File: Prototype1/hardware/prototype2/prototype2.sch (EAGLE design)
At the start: 79 parts, among them IC1 ATTINY13A-SSU, IC2 LDL112D33R, IC3 FT2232HL-REEL, IC4 93LC46BT-I_OT, U2 ESP-WROOM-32

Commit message: prototype 2 schema done(?)
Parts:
- added ATTINY13A: Header, connector:M06SILK_FEMALE_PTH
- added C2: 4.7 uF, passives:C-USC0805
- added C26, C27, C28, C29, C30, C31: 15 pF, passives:C-USC0805
- added C32: 0.1 uF, passives:C-USC0805
- added C33, C34: 10 uF, passives:C-USC0805
- added LED8: (no value), leds:LED3MM
- added R15, R18, R19, R20: 100 R, dc-26:RESISTOR0805-RES
- added R16: 4.7 K, passives:RESISTOR0805-RES
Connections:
- removed net N$12: C4.1, IC2.VIN, RESETTABLE_FUSE.2
- new net ATTINY_ESP_CON: IC1.[PCINT3/CLKI/ADC3]_PB3, R19.1
- new net ESP_ATTINY_CON: R19.2, U2.IO2
- new net ESP_LED1: R20.2, U2.IO16
- new net GPIO_APA104_DATA: IC1.[PCINT4/ADC2]_PB4, U$6.DIN
- new net N$35: U$6.DOUT, U$7.DIN
- new net N$36: U$7.DOUT, U$8.DIN
- new net N$37: U$8.DOUT, U$9.DIN
- new net N$38: U$10.DIN, U$9.DOUT
- new net N$39: U$10.DOUT, U$11.DIN
- new net N$9: LED8.A, R20.1
- new net PB0: ATTINY13A.4, IC1.PB0_[MOSI/AIN0/OC0A/PCINT0]
- new net PB1: ATTINY13A.5, IC1.PB1_[MISO/AIN1/OC0B/INT0/PCINT1]
- new net PB2: ATTINY13A.6, IC1.PB2_[SCK/ADC1/T0/PCINT2]
- new net PB3: ATTINY13A.2
- new net PB4: ATTINY13A.1
- new net PB5: ATTINY13A.3, IC1.PCINT5/!RESET!/ADC0/DW]_PB5, R16.1
- new net VBAT: C26.1, C27.1, C28.1, C29.1, C30.1, C31.1, C32.1, C33.1, C4.1, IC1.VCC, IC2.VIN, R16.2, RESETTABLE_FUSE.2, U$10.VDD, U$11.VDD, U$6.VDD, U$7.VDD, U$8.VDD, U$9.VDD
- net DISPLAY_BACKLIT: now also C34.1, R18.2; no longer U2.IO16
- net DISPLAY_RESET: now also C2.1, R15.2; no longer U2.IO2
- net GND: now also C2.2, C26.2, C27.2, C28.2, C29.2, C30.2, C31.2, C32.2, C33.2, C34.2, IC1.GND, LED8.C, U$10.GND, U$11.GND, U$6.GND, U$7.GND, U$8.GND, U$9.GND
- net VCC: now also R15.1, R18.1
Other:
- note added: "If we don't connect RESX line to a GPIO (and I'm not to save GPIO pins), we need to ensure RESX stay low for 10 us. So I'm going to set it up to stay low via a capacitor for 470 us by using a 4.7 uF cap and a 100 Ohm resistor calculator used: https://www.allaboutcircuits.com/tools/capacitor-Charge-and-time-constant-calculator/ same for back light, except using a larger cap to delay even longer"
- note removed: "If we use UART for badge pairing what pins do I use? Only pins left are input only Can I move MISO to one of these pins? so I can free up output pins? Need 2 more output Pins 1 for BADGE_PAIR_TX and 1 for ATTINY"
- moved on the sheet: IC1, U$10, U$11, U$6, U$7, U$8, U$9

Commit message: fixed erc errors and warnings
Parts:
- added J4: (no value), connector:M04PTH
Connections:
- removed net N$22: R2.1
- removed net N$23: C13.2
- removed net N$4: OFF/ON.S
- removed net PB3: ATTINY13A.2
- removed net PB4: ATTINY13A.1
- removed net PROX_RX: R14.1
- removed net RXD-SPI_PROM_MOSI: IC3.BDBUS1
- removed net SENSORVN: U2.SENSOR_VN
- removed net SENSORVP: U2.SENSOR_VP
- removed net TXD-SPI_PROM_CLK: IC3.BDBUS0
- new net SVN: J4.1, U2.SENSOR_VN
- new net SVP: J4.2, U2.SENSOR_VP
- net ATTINY_ESP_CON: now also ATTINY13A.2
- net GND: now also C25.2
- net GPIO_APA104_DATA: now also ATTINY13A.1
- net PAIR_RX: now also J4.4
- net PAIR_TX: now also J4.3
- net PROG_RX: now also R14.1
- net RXD_SPI_PROM_MOSI: now also IC3.BDBUS1
- net TXD_SPI_PROM_CLK: now also IC3.BDBUS0
- net VBAT: now also OFF/ON.S
- net VCC5V: now also C13.2, R2.1
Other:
- moved on the sheet: C13, C22, R2

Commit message: fixed one more warning
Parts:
- J4: value (none) -> DN PAIR
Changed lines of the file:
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@@
 <part name="LED8" library="leds" deviceset="LED" device="3MM"/>
 <part name="R20" library="dc-26" deviceset="RESISTOR" device="0805-RES" value="100 R"/>
-<part name="J4" library="connector" deviceset="M04" device="PTH"/>
+<part name="J4" library="connector" deviceset="M04" device="PTH" value="DN PAIR"/>
 </parts>
 <sheets>

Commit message: prototype 2 board design 'complete'
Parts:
- removed C30, C31: 15 pF, passives:C-USC0805
- removed U$10, U$11, U$6, U$7, U$8, U$9: APA-106, leds:APA-106
- added C35: 0.1 uF, passives:C-USC0805
- added IC5, IC6, IC7, IC8: APA104, leds:APA104
- R2: value 2 R -> 10 R
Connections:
- removed net N$35: U$6.DOUT, U$7.DIN
- removed net N$36: U$7.DOUT, U$8.DIN
- removed net N$37: U$8.DOUT, U$9.DIN
- removed net N$38: U$10.DIN, U$9.DOUT
- removed net N$39: U$10.DOUT, U$11.DIN
- new net N$12: IC6.DOUT, IC7.DIN
- new net N$22: IC7.DOUT, IC8.DIN
- new net N$4: IC5.DOUT, IC6.DIN
- net GND: now also C35.2, IC5.VSS, IC6.VSS, IC7.VSS, IC8.VSS; no longer C30.2, C31.2, U$10.GND, U$11.GND, U$6.GND, U$7.GND, U$8.GND, U$9.GND
- net GPIO_APA104_DATA: now also IC5.DIN; no longer U$6.DIN
- net N$14: now also IC-IP5305.3
- net PAIR_RX: now also J4.2; no longer J4.4
- net PAIR_TX: now also J4.1; no longer J4.3
- net PB0: now also ATTINY13A.6; no longer ATTINY13A.4
- net PB2: now also ATTINY13A.4; no longer ATTINY13A.6
- net PROG_RX: no longer J1.10
- net PROG_TX: no longer J1.11
- net RXD_SPI_PROM_MOSI: now also J1.11
- net SVN: now also J4.3; no longer J4.1
- net SVP: now also J4.4; no longer J4.2
- net TOUCH_DATA_IN: now also J8.6; no longer J8.4
- net TOUCH_DATA_OUT: now also J8.4; no longer J8.5
- net TOUCH_IRQ: now also J8.5; no longer J8.6
- net TXD_SPI_PROM_CLK: now also J1.10
- net VBAT: now also IC5.VDD, IC6.VDD, IC7.VDD, IC8.VDD; no longer C30.1, C31.1, U$10.VDD, U$11.VDD, U$6.VDD, U$7.VDD, U$8.VDD, U$9.VDD
- net VCC: now also C35.1
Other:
- moved on the sheet: C26, C27, C28, C29

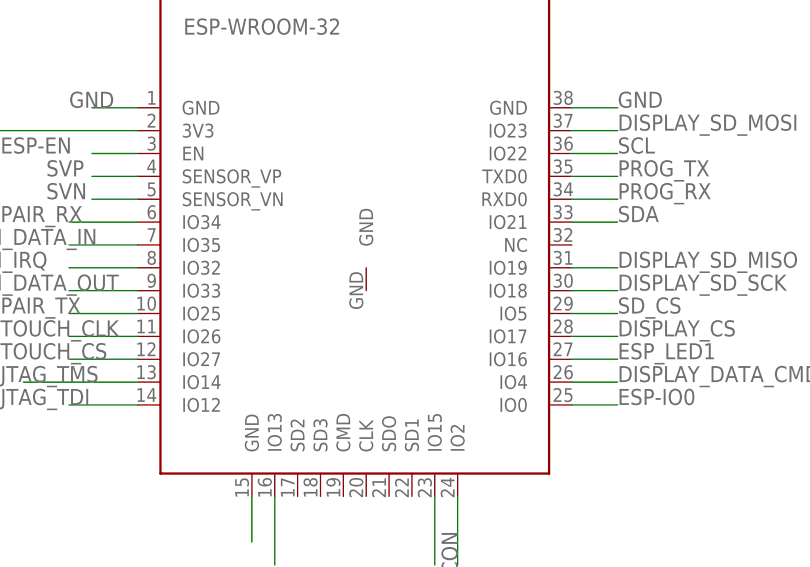
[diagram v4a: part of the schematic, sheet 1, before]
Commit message: fixed bug with center ground plane on esp32
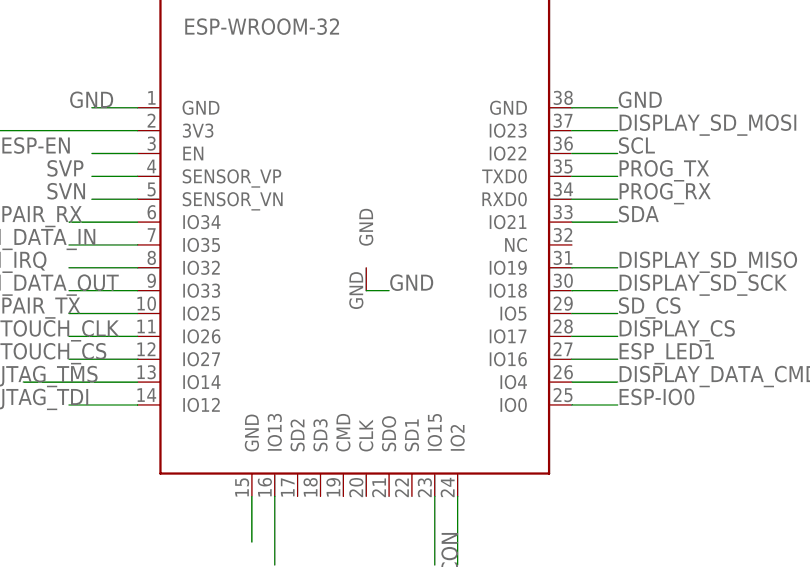
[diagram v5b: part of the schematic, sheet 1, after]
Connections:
- net GND: now also U2.GND
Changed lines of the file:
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@@
 <label x="195.58" y="71.12" size="1.778" layer="95"/>
+</segment>
+<segment>
+<pinref part="U2" gate="G$1" pin="GND"/>
+<wire x1="81.28" y1="38.1" x2="83.82" y2="38.1" width="0.1524" layer="91"/>
+<label x="83.82" y="38.1" size="1.778" layer="95"/>
 </segment>
 </net>

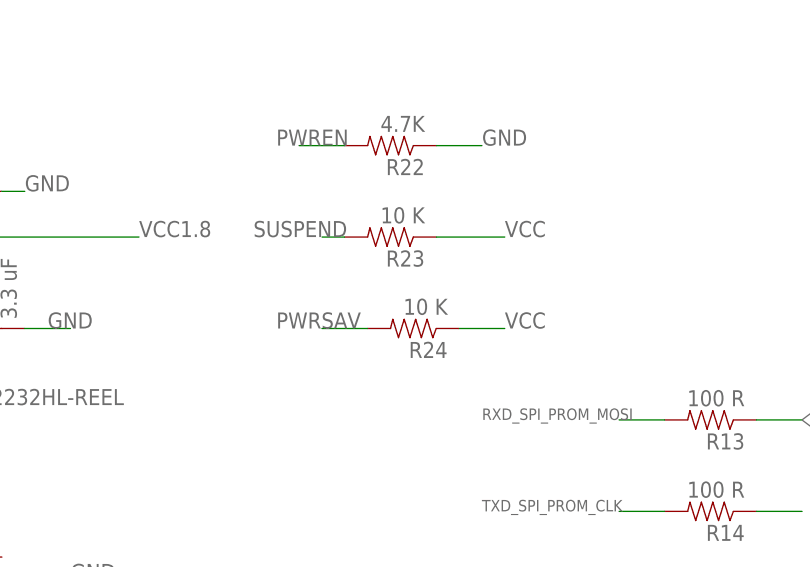
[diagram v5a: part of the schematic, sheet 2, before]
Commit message: removed inputs to output pins....duh
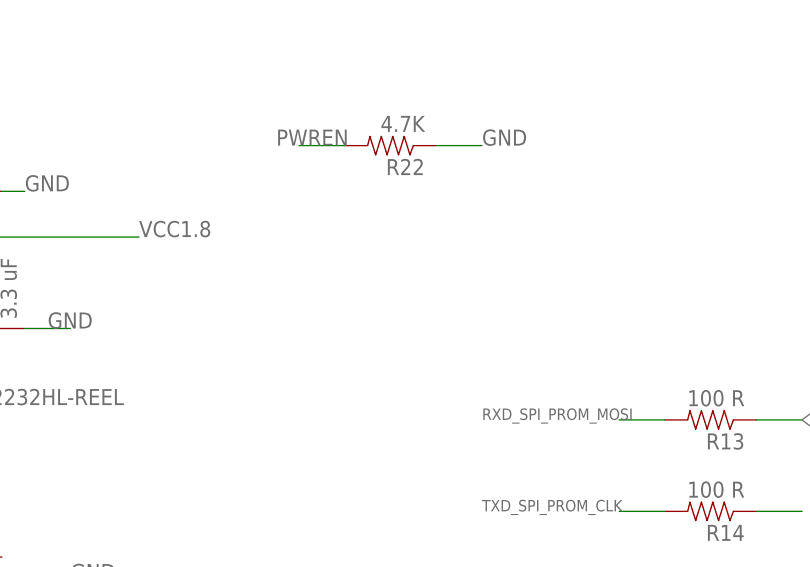
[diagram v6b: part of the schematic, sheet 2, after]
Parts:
- removed R23, R24: 10 K, passives:RESISTOR0805-RES
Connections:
- net PWRSAV: no longer R24.2
- net SUSPEND: no longer R23.2
- net VCC: no longer R23.1, R24.1
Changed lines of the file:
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@@
 <part name="D1" library="passives" deviceset="DIODE" device="SMA"/>
 <part name="R22" library="passives" deviceset="RESISTOR" device="0805-RES" value="4.7K"/>
-<part name="R23" library="passives" deviceset="RESISTOR" device="0805-RES" value="10 K"/>
-<part name="R24" library="passives" deviceset="RESISTOR" device="0805-RES" value="10 K"/>
 <part name="J8" library="connector" deviceset="M06" device="NO_SILK_YES_STOP"/>
 <part name="J1" library="connector" deviceset="M14" device=""/>
@@
 <attribute name="VALUE" x="130.81" y="115.062" size="1.778" layer="96" rot="R180"/>
 </instance>
-<instance part="R23" gate="G$1" x="127" y="101.6" smashed="yes" rot="R180">
-<attribute name="NAME" x="130.81" y="100.1014" size="1.778" layer="95" rot="R180"/>
-<attribute name="VALUE" x="130.81" y="104.902" size="1.778" layer="96" rot="R180"/>
-</instance>
-<instance part="R24" gate="G$1" x="129.54" y="91.44" smashed="yes" rot="R180">
-<attribute name="NAME" x="133.35" y="89.9414" size="1.778" layer="95" rot="R180"/>
-<attribute name="VALUE" x="133.35" y="94.742" size="1.778" layer="96" rot="R180"/>
-</instance>
 <instance part="C3" gate="G$1" x="22.86" y="149.86" smashed="yes" rot="R270">
 <attribute name="NAME" x="23.495" y="156.464" size="1.778" layer="95" rot="R270"/>
@@
 <wire x1="-73.66" y1="27.94" x2="-83.82" y2="27.94" width="0.1524" layer="91"/>
 <label x="-83.82" y="27.94" size="1.778" layer="95"/>
-</segment>
-<segment>
-<pinref part="R23" gate="G$1" pin="1"/>
-<wire x1="132.08" y1="101.6" x2="139.7" y2="101.6" width="0.1524" layer="91"/>
-<label x="139.7" y="101.6" size="1.778" layer="95"/>
-</segment>
-<segment>
-<pinref part="R24" gate="G$1" pin="1"/>
-<wire x1="134.62" y1="91.44" x2="139.7" y2="91.44" width="0.1524" layer="91"/>
-<label x="139.7" y="91.44" size="1.778" layer="95"/>
 </segment>
 <segment>
@@
 <label x="91.44" y="35.56" size="1.778" layer="95"/>
 </segment>
-<segment>
-<pinref part="R23" gate="G$1" pin="2"/>
-<wire x1="121.92" y1="101.6" x2="119.38" y2="101.6" width="0.1524" layer="91"/>
-<label x="111.76" y="101.6" size="1.778" layer="95"/>
-</segment>
 </net>
 <net name="PWRSAV" class="0">
@@
 <label x="50.8" y="88.9" size="1.778" layer="95" rot="R90"/>
 </segment>
-<segment>
-<pinref part="R24" gate="G$1" pin="2"/>
-<wire x1="124.46" y1="91.44" x2="119.38" y2="91.44" width="0.1524" layer="91"/>
-<label x="114.3" y="91.44" size="1.778" layer="95"/>
-</segment>
-</net>
+</net>
